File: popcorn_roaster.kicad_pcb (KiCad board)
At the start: 2 copper layers, 105.8 x 77.9 mm, 40 parts, among them Q1 BC847B, U1 R-78K3.3-0.5, U2 IRM-45-24, U3 MOC3063S, U4 MAX31855

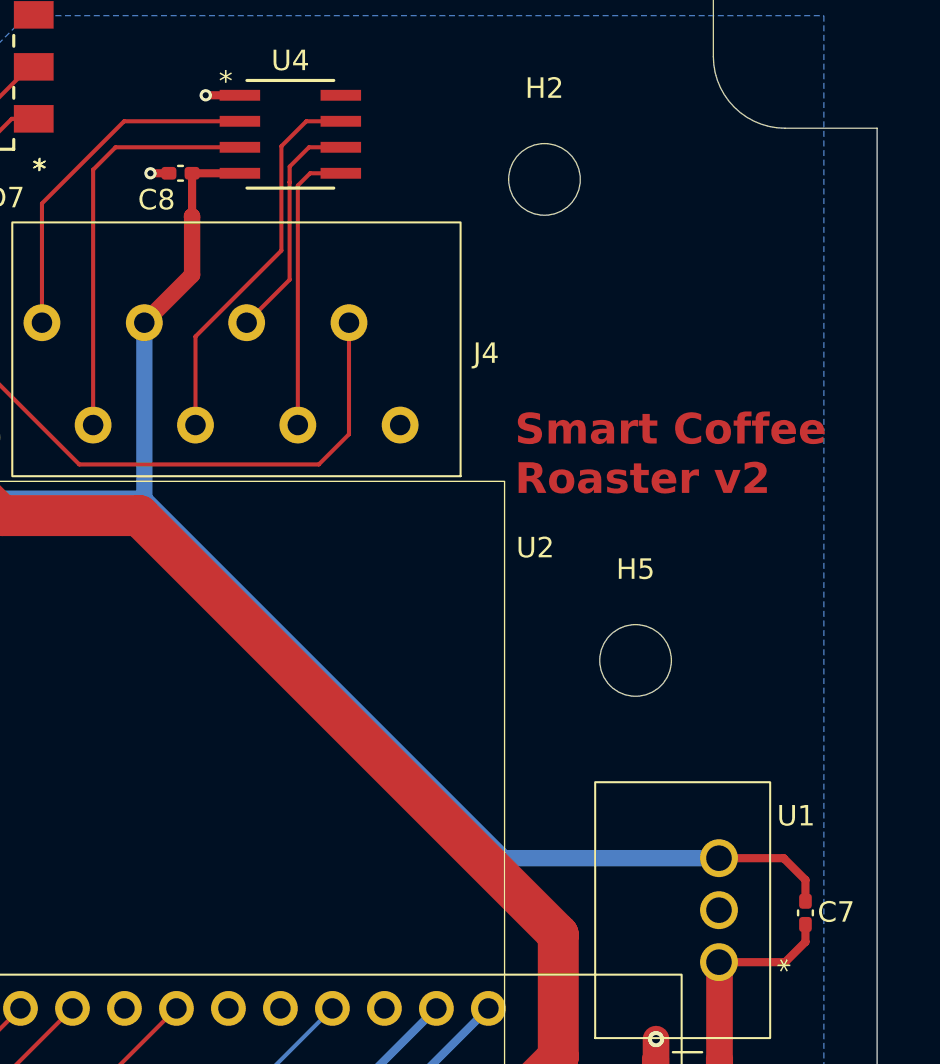
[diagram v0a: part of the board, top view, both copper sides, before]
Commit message: Use larger package for capacitors
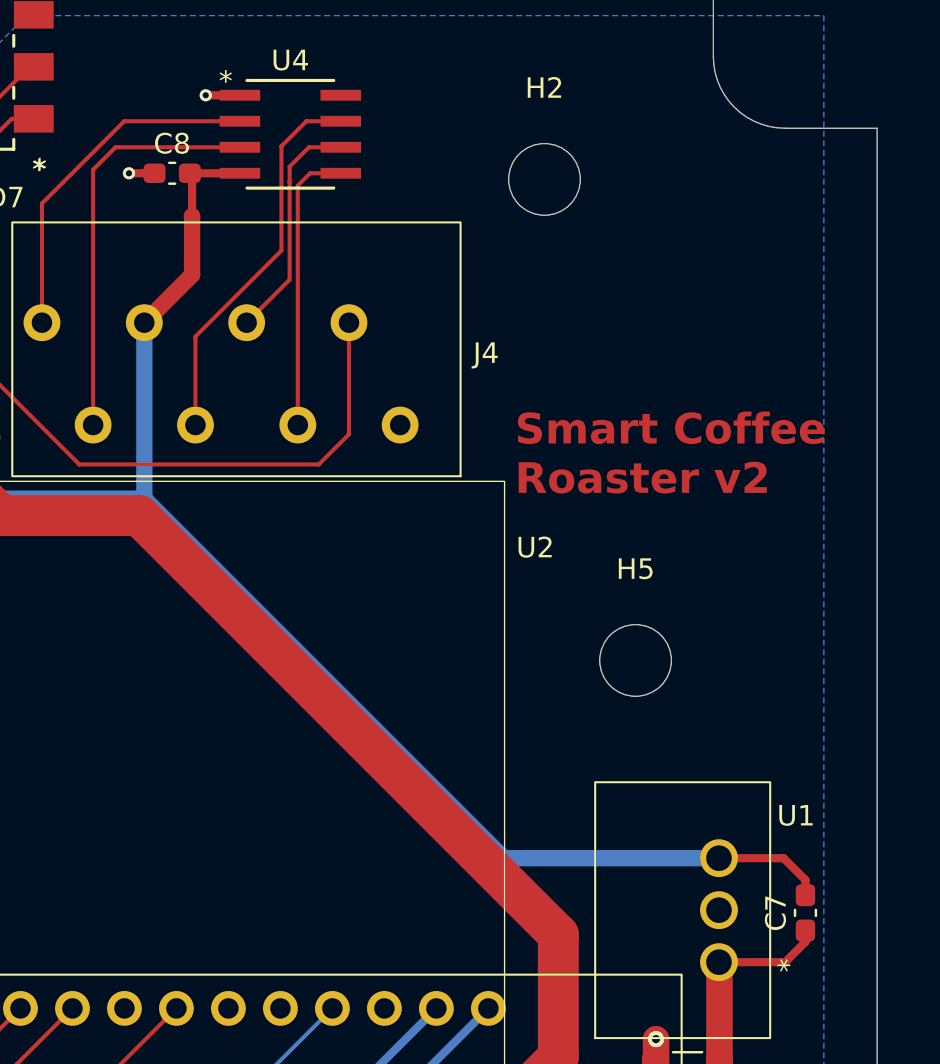
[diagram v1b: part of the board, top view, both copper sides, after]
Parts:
- C7, C8: footprint Capacitor_SMD:C_0402_1005Metric_Pad0.74x0.62mm_HandSolder -> Capacitor_SMD:C_0603_1608Metric_Pad1.08x0.95mm_HandSolder
- R7: value 6K2 -> 10K0
- moved C8 0.41 mm to (71.4, 10.2)
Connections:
- net Net-(D6-A2) renamed /Smart Roaster/heat_black
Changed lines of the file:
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@@
 	(net 17 "unconnected-(U4-DNC-Pad8)")
 	(net 18 "/Smart Roaster/heat_blue")
-	(net 19 "Net-(D6-A2)")
+	(net 19 "/Smart Roaster/heat_black")
 	(net 20 "Net-(D7-A)")
 	(net 21 "Net-(J3-Pin_1)")
@@
 		)
 	)
-	(footprint "Capacitor_SMD:C_0402_1005Metric_Pad0.74x0.62mm_HandSolder"
+	(footprint "Capacitor_SMD:C_0603_1608Metric_Pad1.08x0.95mm_HandSolder"
 		(layer "F.Cu")
-		(at 71.7675 10.2)
-		(descr "Capacitor SMD 0402 (1005 Metric), square (rectangular) end terminal, IPC-7351 nominal with elongated pad for handsoldering. (Body size source: IPC-SM-782 page 76, https://www.pcb-3d.com/wordpress/wp-content/uploads/ipc-sm-782a_amendment_1_and_2.pdf), generated with kicad-footprint-generator")
+		(at 71.3625 10.2)
+		(descr "Capacitor SMD 0603 (1608 Metric), square (rectangular) end terminal, IPC-7351 nominal with elongated pad for handsoldering. (Body size source: IPC-SM-782 page 76, https://www.pcb-3d.com/wordpress/wp-content/uploads/ipc-sm-782a_amendment_1_and_2.pdf), generated with kicad-footprint-generator")
 		(tags "capacitor handsolder")
 		(property "Reference" "C8"
-			(at -1.1675 1.3 180)
+			(at 0 -1.43 0)
 			(layer "F.SilkS")
 			(effects
@@
 		)
 		(property "Value" "100nF"
-			(at 3.5675 0 0)
+			(at 0 1.43 0)
 			(layer "F.Fab")
 			(effects
@@
 		(property "Datasheet" ""
 			(at 0 0 0)
-			(unlocked yes)
 			(layer "F.Fab")
 			(hide yes)
@@
 		(property "Description" "Unpolarized capacitor"
 			(at 0 0 0)
-			(unlocked yes)
 			(layer "F.Fab")
 			(hide yes)
@@
 		(attr smd)
 		(fp_line
-			(start -0.115835 -0.36)
-			(end 0.115835 -0.36)
+			(start -0.146267 -0.51)
+			(end 0.146267 -0.51)
 			(stroke
 				(width 0.12)
@@
 		)
 		(fp_line
-			(start -0.115835 0.36)
-			(end 0.115835 0.36)
+			(start -0.146267 0.51)
+			(end 0.146267 0.51)
 			(stroke
 				(width 0.12)
@@
 		)
 		(fp_line
-			(start -1.09 -0.46)
-			(end 1.09 -0.46)
+			(start -1.65 -0.73)
+			(end 1.65 -0.73)
 			(stroke
 				(width 0.05)
@@
 		)
 		(fp_line
-			(start -1.09 0.46)
-			(end -1.09 -0.46)
+			(start -1.65 0.73)
+			(end -1.65 -0.73)
 			(stroke
 				(width 0.05)
@@
 		)
 		(fp_line
-			(start 1.09 -0.46)
-			(end 1.09 0.46)
+			(start 1.65 -0.73)
+			(end 1.65 0.73)
 			(stroke
 				(width 0.05)
@@
 		)
 		(fp_line
-			(start 1.09 0.46)
-			(end -1.09 0.46)
+			(start 1.65 0.73)
+			(end -1.65 0.73)
 			(stroke
 				(width 0.05)
@@
 		)
 		(fp_line
-			(start -0.5 -0.25)
-			(end 0.5 -0.25)
+			(start -0.8 -0.4)
+			(end 0.8 -0.4)
 			(stroke
 				(width 0.1)
@@
 		)
 		(fp_line
-			(start -0.5 0.25)
-			(end -0.5 -0.25)
+			(start -0.8 0.4)
+			(end -0.8 -0.4)
 			(stroke
 				(width 0.1)
@@
 		)
 		(fp_line
-			(start 0.5 -0.25)
-			(end 0.5 0.25)
+			(start 0.8 -0.4)
+			(end 0.8 0.4)
 			(stroke
 				(width 0.1)
@@
 		)
 		(fp_line
-			(start 0.5 0.25)
-			(end -0.5 0.25)
+			(start 0.8 0.4)
+			(end -0.8 0.4)
 			(stroke
 				(width 0.1)
@@
 			(effects
 				(font
-					(size 0.25 0.25)
-					(thickness 0.04)
+					(size 0.4 0.4)
+					(thickness 0.06)
 				)
 			)
 		)
 		(pad "1" smd roundrect
-			(at -0.5675 0)
-			(size 0.735 0.62)
+			(at -0.8625 0)
+			(size 1.075 0.95)
 			(layers "F.Cu" "F.Mask" "F.Paste")
 			(roundrect_rratio 0.25)
@@
 		)
 		(pad "2" smd roundrect
-			(at 0.5675 0)
-			(size 0.735 0.62)
+			(at 0.8625 0)
+			(size 1.075 0.95)
 			(layers "F.Cu" "F.Mask" "F.Paste")
 			(roundrect_rratio 0.25)
@@
 		)
 		(embedded_fonts no)
-		(model "${KICAD9_3DMODEL_DIR}/Capacitor_SMD.3dshapes/C_0402_1005Metric.step"
+		(model "${KICAD9_3DMODEL_DIR}/Capacitor_SMD.3dshapes/C_0603_1608Metric.step"
 			(offset
 				(xyz 0 0 0)
@@
 		)
 	)
-	(footprint "Capacitor_SMD:C_0402_1005Metric_Pad0.74x0.62mm_HandSolder"
+	(footprint "Capacitor_SMD:C_0603_1608Metric_Pad1.08x0.95mm_HandSolder"
 		(layer "F.Cu")
 		(at 102.3 46.3325 90)
-		(descr "Capacitor SMD 0402 (1005 Metric), square (rectangular) end terminal, IPC-7351 nominal with elongated pad for handsoldering. (Body size source: IPC-SM-782 page 76, https://www.pcb-3d.com/wordpress/wp-content/uploads/ipc-sm-782a_amendment_1_and_2.pdf), generated with kicad-footprint-generator")
+		(descr "Capacitor SMD 0603 (1608 Metric), square (rectangular) end terminal, IPC-7351 nominal with elongated pad for handsoldering. (Body size source: IPC-SM-782 page 76, https://www.pcb-3d.com/wordpress/wp-content/uploads/ipc-sm-782a_amendment_1_and_2.pdf), generated with kicad-footprint-generator")
 		(tags "capacitor handsolder")
 		(property "Reference" "C7"
-			(at 0.0325 1.5 180)
+			(at 0 -1.43 90)
 			(layer "F.SilkS")
 			(effects
@@
 		)
 		(property "Value" "1nF"
-			(at 0 1.16 90)
+			(at 0 1.43 90)
 			(layer "F.Fab")
 			(effects
@@
 		(property "Datasheet" ""
 			(at 0 0 90)
-			(unlocked yes)
 			(layer "F.Fab")
 			(hide yes)
@@
 		(property "Description" "Unpolarized capacitor"
 			(at 0 0 90)
-			(unlocked yes)
 			(layer "F.Fab")
 			(hide yes)
@@
 		(attr smd)
 		(fp_line
-			(start -0.115835 -0.36)
-			(end 0.115835 -0.36)
+			(start -0.146267 -0.51)
+			(end 0.146267 -0.51)
 			(stroke
 				(width 0.12)
@@
 		)
 		(fp_line
-			(start -0.115835 0.36)
-			(end 0.115835 0.36)
+			(start -0.146267 0.51)
+			(end 0.146267 0.51)
 			(stroke
 				(width 0.12)
@@
 		)
 		(fp_line
-			(start 1.09 -0.46)
-			(end 1.09 0.46)
+			(start 1.65 -0.73)
+			(end 1.65 0.73)
 			(stroke
 				(width 0.05)
@@
 		)
 		(fp_line
-			(start -1.09 -0.46)
-			(end 1.09 -0.46)
+			(start -1.65 -0.73)
+			(end 1.65 -0.73)
 			(stroke
 				(width 0.05)
@@
 		)
 		(fp_line
-			(start 1.09 0.46)
-			(end -1.09 0.46)
+			(start 1.65 0.73)
+			(end -1.65 0.73)
 			(stroke
 				(width 0.05)
@@
 		)
 		(fp_line
-			(start -1.09 0.46)
-			(end -1.09 -0.46)
+			(start -1.65 0.73)
+			(end -1.65 -0.73)
 			(stroke
 				(width 0.05)
@@
 		)
 		(fp_line
-			(start 0.5 -0.25)
-			(end 0.5 0.25)
+			(start 0.8 -0.4)
+			(end 0.8 0.4)
 			(stroke
 				(width 0.1)
@@
 		)
 		(fp_line
-			(start -0.5 -0.25)
-			(end 0.5 -0.25)
+			(start -0.8 -0.4)
+			(end 0.8 -0.4)
 			(stroke
 				(width 0.1)
@@
 		)
 		(fp_line
-			(start 0.5 0.25)
-			(end -0.5 0.25)
+			(start 0.8 0.4)
+			(end -0.8 0.4)
 			(stroke
 				(width 0.1)
@@
 		)
 		(fp_line
-			(start -0.5 0.25)
-			(end -0.5 -0.25)
+			(start -0.8 0.4)
+			(end -0.8 -0.4)
 			(stroke
 				(width 0.1)
@@
 			(effects
 				(font
-					(size 0.25 0.25)
-					(thickness 0.04)
+					(size 0.4 0.4)
+					(thickness 0.06)
 				)
 			)
 		)
 		(pad "1" smd roundrect
-			(at -0.5675 0 90)
-			(size 0.735 0.62)
+			(at -0.8625 0 90)
+			(size 1.075 0.95)
 			(layers "F.Cu" "F.Mask" "F.Paste")
 			(roundrect_rratio 0.25)
@@
 		)
 		(pad "2" smd roundrect
-			(at 0.5675 0 90)
-			(size 0.735 0.62)
+			(at 0.8625 0 90)
+			(size 1.075 0.95)
 			(layers "F.Cu" "F.Mask" "F.Paste")
 			(roundrect_rratio 0.25)
@@
 		)
 		(embedded_fonts no)
-		(model "${KICAD9_3DMODEL_DIR}/Capacitor_SMD.3dshapes/C_0402_1005Metric.step"
+		(model "${KICAD9_3DMODEL_DIR}/Capacitor_SMD.3dshapes/C_0603_1608Metric.step"
 			(offset
 				(xyz 0 0 0)
@@
 			(layers "*.Cu" "*.Mask")
 			(remove_unused_layers no)
-			(net 19 "Net-(D6-A2)")
+			(net 19 "/Smart Roaster/heat_black")
 			(pinfunction "A2")
 			(pintype "passive")
@@
 			(layers "*.Cu" "*.Mask")
 			(remove_unused_layers no)
-			(net 19 "Net-(D6-A2)")
+			(net 19 "/Smart Roaster/heat_black")
 			(pinfunction "1")
 			(pintype "passive")
@@
 			(layers "*.Cu" "*.Mask")
 			(remove_unused_layers no)
-			(net 19 "Net-(D6-A2)")
+			(net 19 "/Smart Roaster/heat_black")
 			(pinfunction "AC_L")
 			(pintype "power_in")
@@
 			)
 		)
-		(property "Value" "6K2"
+		(property "Value" "10K0"
 			(at 0 1.43 0)
 			(layer "F.Fab")
@@
 			(layers "F.Cu" "F.Mask" "F.Paste")
 			(roundrect_rratio 0.25)
-			(net 19 "Net-(D6-A2)")
+			(net 19 "/Smart Roaster/heat_black")
 			(pintype "passive")
 		)
@@
 	)
 	(segment
-		(start 70.3 10.2)
-		(end 71.2 10.2)
-		(width 0.4)
+		(start 59.25 14.1)
+		(end 59.25 16.4)
+		(width 0.2)
 		(layer "F.Cu")
 		(net 2)
 	)
 	(segment
-		(start 59.25 14.1)
-		(end 59.25 16.4)
-		(width 0.2)
+		(start 69.25 10.2)
+		(end 70.5 10.2)
+		(width 0.4)
 		(layer "F.Cu")
 		(net 2)
@@
 	)
 	(via
-		(at 70.3 10.2)
+		(at 69.25 10.2)
 		(size 0.6)
 		(drill 0.3)

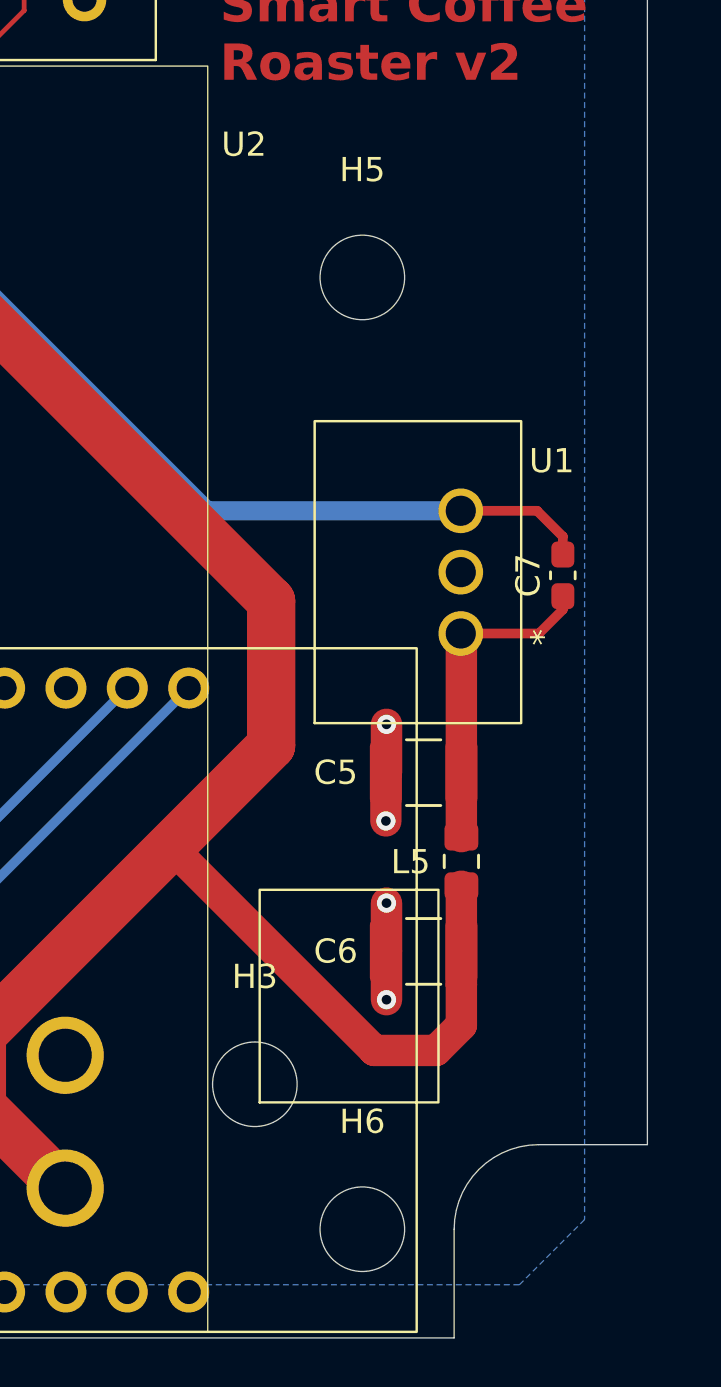
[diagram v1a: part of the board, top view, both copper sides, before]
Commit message: Remove unnecessary mounting holes
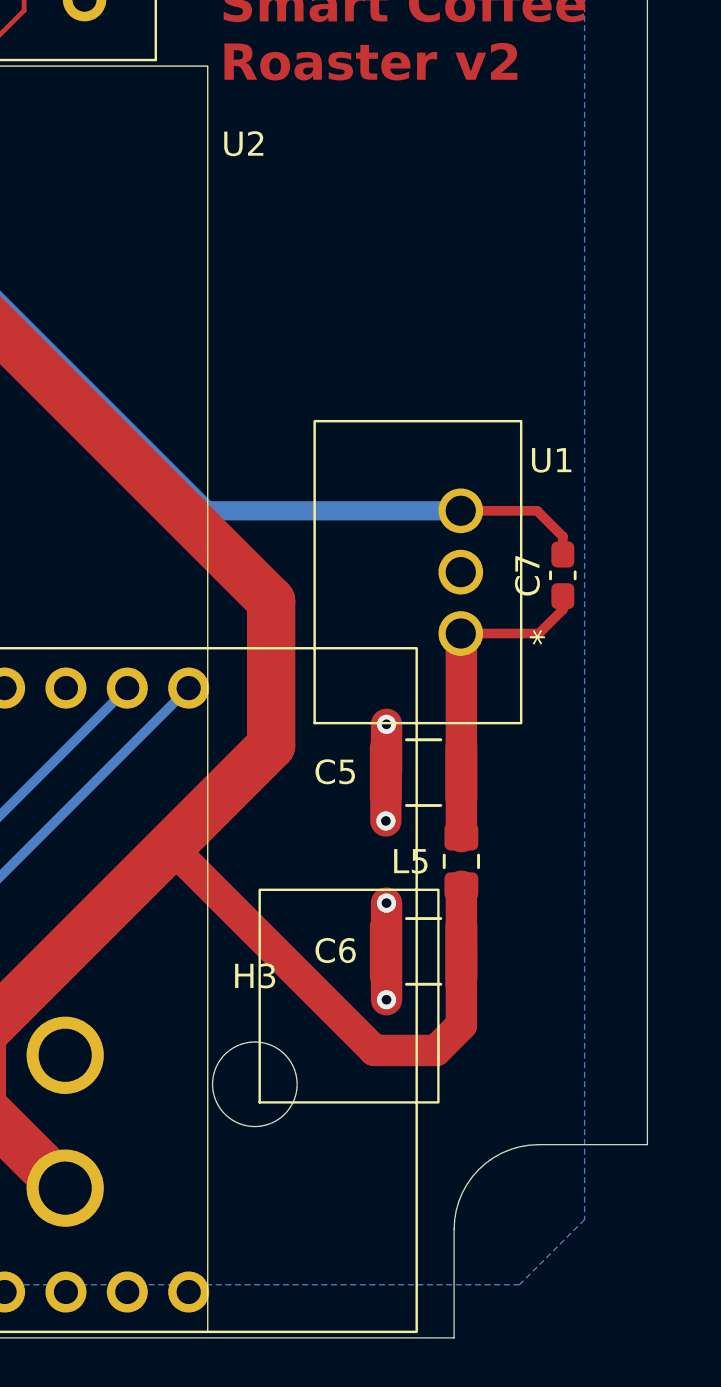
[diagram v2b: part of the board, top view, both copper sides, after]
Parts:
- removed H5, H6: MountingHole, MountingHole:MountingHole_3.5mm
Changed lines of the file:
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@@
 		)
 	)
-	(footprint "MountingHole:MountingHole_3.5mm"
-		(layer "F.Cu")
-		(at 94 34)
-		(descr "Mounting Hole 3.5mm, no annular, generated by kicad-footprint-generator mountinghole.py")
-		(tags "mountinghole")
-		(property "Reference" "H5"
-			(at 0 -4.45 0)
-			(layer "F.SilkS")
-			(effects
-				(font
-					(size 1 1)
-					(thickness 0.15)
-				)
-			)
-		)
-		(property "Value" "MountingHole"
-			(at 0 4.45 0)
-			(layer "F.Fab")
-			(effects
-				(font
-					(size 1 1)
-					(thickness 0.15)
-				)
-			)
-		)
-		(property "Datasheet" ""
-			(at 0 0 0)
-			(layer "F.Fab")
-			(hide yes)
-			(effects
-				(font
-					(size 1.27 1.27)
-					(thickness 0.15)
-				)
-			)
-		)
-		(property "Description" "Mounting Hole without connection"
-			(at 0 0 0)
-			(layer "F.Fab")
-			(hide yes)
-			(effects
-				(font
-					(size 1.27 1.27)
-					(thickness 0.15)
-				)
-			)
-		)
-		(property ki_fp_filters "MountingHole*")
-		(sheetname "/Smart Roaster/")
-		(sheetfile "smart_roaster.kicad_sch")
-		(attr exclude_from_pos_files exclude_from_bom)
-		(fp_circle
-			(center 0 0)
-			(end 3.5 0)
-			(stroke
-				(width 0.15)
-				(type solid)
-			)
-			(fill no)
-			(layer "Cmts.User")
-		)
-		(fp_circle
-			(center 0 0)
-			(end 3.75 0)
-			(stroke
-				(width 0.05)
-				(type solid)
-			)
-			(fill no)
-			(layer "F.CrtYd")
-		)
-		(fp_text user "${REFERENCE}"
-			(at 0 0 0)
-			(layer "F.Fab")
-			(effects
-				(font
-					(size 1 1)
-					(thickness 0.15)
-				)
-			)
-		)
-		(pad "" np_thru_hole circle
-			(at 0 0)
-			(size 3.5 3.5)
-			(drill 3.5)
-			(layers "*.Cu" "*.Mask")
-		)
-		(embedded_fonts no)
-	)
 	(footprint "Capacitor_SMD:C_1210_3225Metric_Pad1.33x2.70mm_HandSolder"
 		(layer "F.Cu")
@@
 		)
 	)
-	(footprint "MountingHole:MountingHole_3.5mm"
-		(layer "F.Cu")
-		(at 94 73.4)
-		(descr "Mounting Hole 3.5mm, no annular, generated by kicad-footprint-generator mountinghole.py")
-		(tags "mountinghole")
-		(property "Reference" "H6"
-			(at 0 -4.45 0)
-			(layer "F.SilkS")
-			(effects
-				(font
-					(size 1 1)
-					(thickness 0.15)
-				)
-			)
-		)
-		(property "Value" "MountingHole"
-			(at 0 4.45 0)
-			(layer "F.Fab")
-			(effects
-				(font
-					(size 1 1)
-					(thickness 0.15)
-				)
-			)
-		)
-		(property "Datasheet" ""
-			(at 0 0 0)
-			(layer "F.Fab")
-			(hide yes)
-			(effects
-				(font
-					(size 1.27 1.27)
-					(thickness 0.15)
-				)
-			)
-		)
-		(property "Description" "Mounting Hole without connection"
-			(at 0 0 0)
-			(layer "F.Fab")
-			(hide yes)
-			(effects
-				(font
-					(size 1.27 1.27)
-					(thickness 0.15)
-				)
-			)
-		)
-		(property ki_fp_filters "MountingHole*")
-		(sheetname "/Smart Roaster/")
-		(sheetfile "smart_roaster.kicad_sch")
-		(attr exclude_from_pos_files exclude_from_bom)
-		(fp_circle
-			(center 0 0)
-			(end 3.5 0)
-			(stroke
-				(width 0.15)
-				(type solid)
-			)
-			(fill no)
-			(layer "Cmts.User")
-		)
-		(fp_circle
-			(center 0 0)
-			(end 3.75 0)
-			(stroke
-				(width 0.05)
-				(type solid)
-			)
-			(fill no)
-			(layer "F.CrtYd")
-		)
-		(fp_text user "${REFERENCE}"
-			(at 0 0 0)
-			(layer "F.Fab")
-			(effects
-				(font
-					(size 1 1)
-					(thickness 0.15)
-				)
-			)
-		)
-		(pad "" np_thru_hole circle
-			(at 0 0)
-			(size 3.5 3.5)
-			(drill 3.5)
-			(layers "*.Cu" "*.Mask")
-		)
-		(embedded_fonts no)
-	)
 	(footprint "TestPoint:TestPoint_THTPad_D2.0mm_Drill1.0mm"
